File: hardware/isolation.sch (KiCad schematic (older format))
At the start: 30 parts

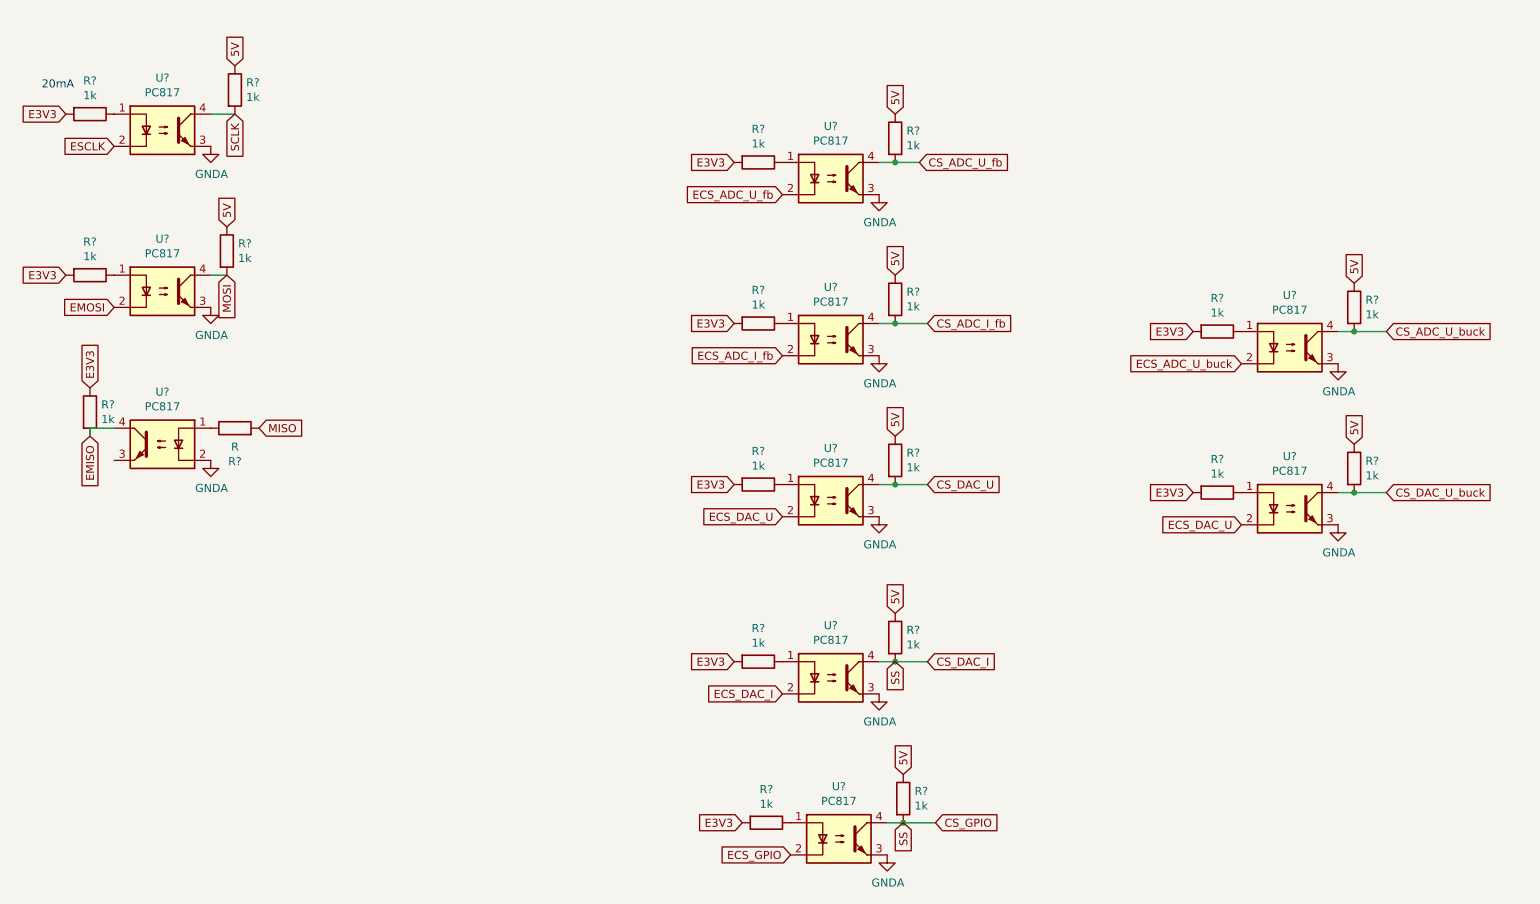
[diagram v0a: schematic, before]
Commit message: switched to xl4016 and worked on control board
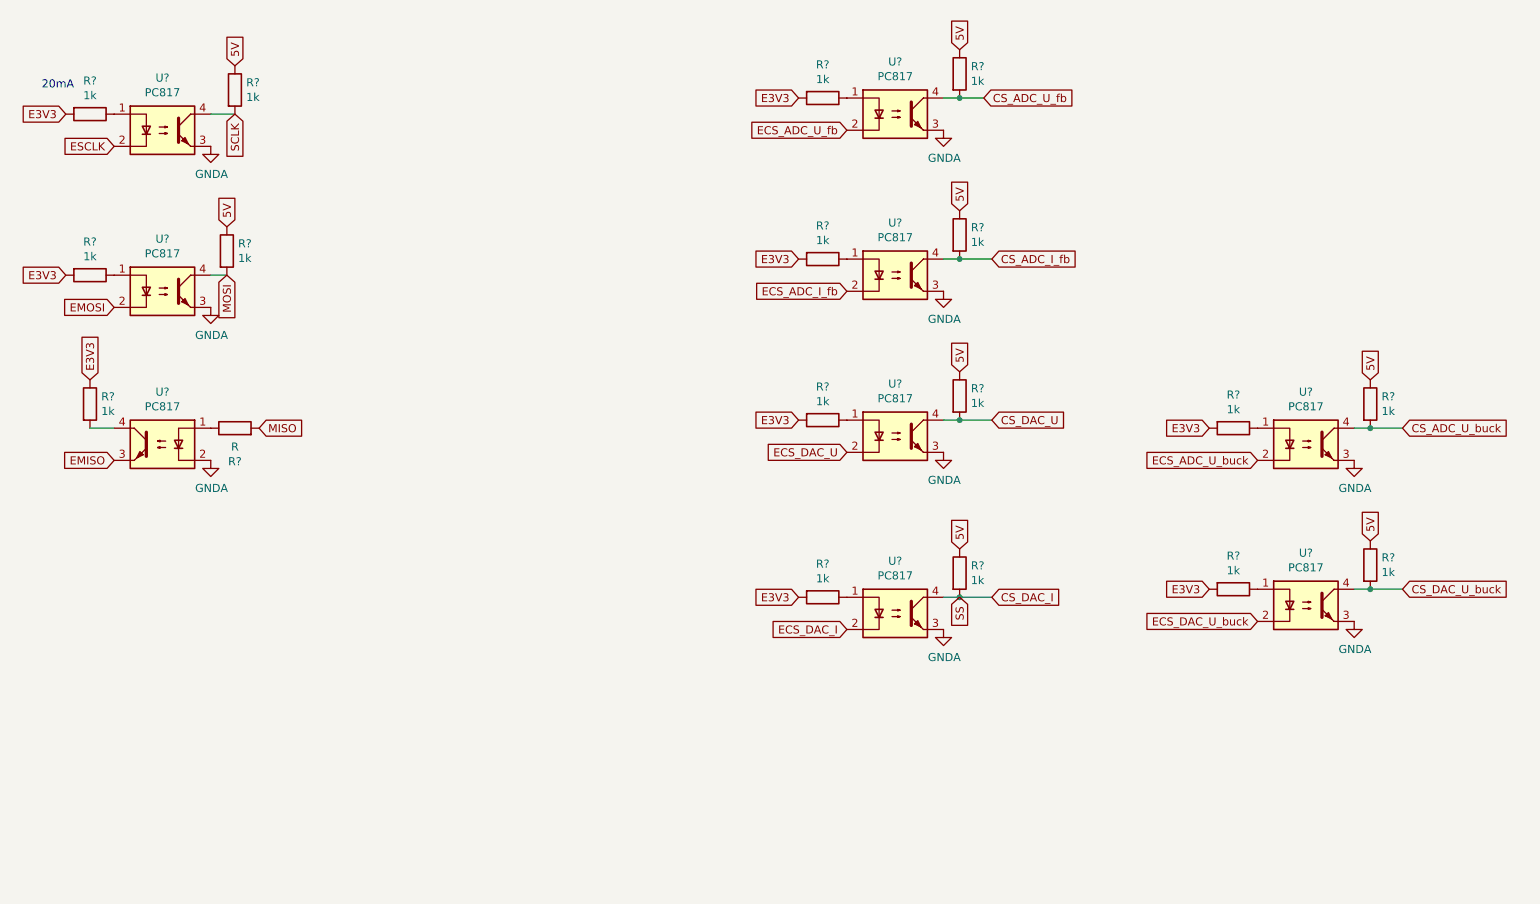
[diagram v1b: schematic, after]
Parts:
- removed R? (x2): 1k, symbol Device:R
- removed U?: PC817, Package_DIP:DIP-4_W7.62mm, symbol Isolator:PC817
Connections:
- net ECS_DAC_U: no longer U?.2
- net EMISO: now also U?.3; no longer R?.2, U?.4
- new net: R?.2, U?.4
- new net ECS_DAC_U_buck: U?.2
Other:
- moved on the sheet: R?, U?
